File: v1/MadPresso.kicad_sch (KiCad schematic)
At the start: 38 parts, among them J1 Conn_01x07, J2 Conn_01x03, Q1 2N7002, Q2 2N7002, Q3 BC847, U1 LTV-356T, U2 WeMos_mini

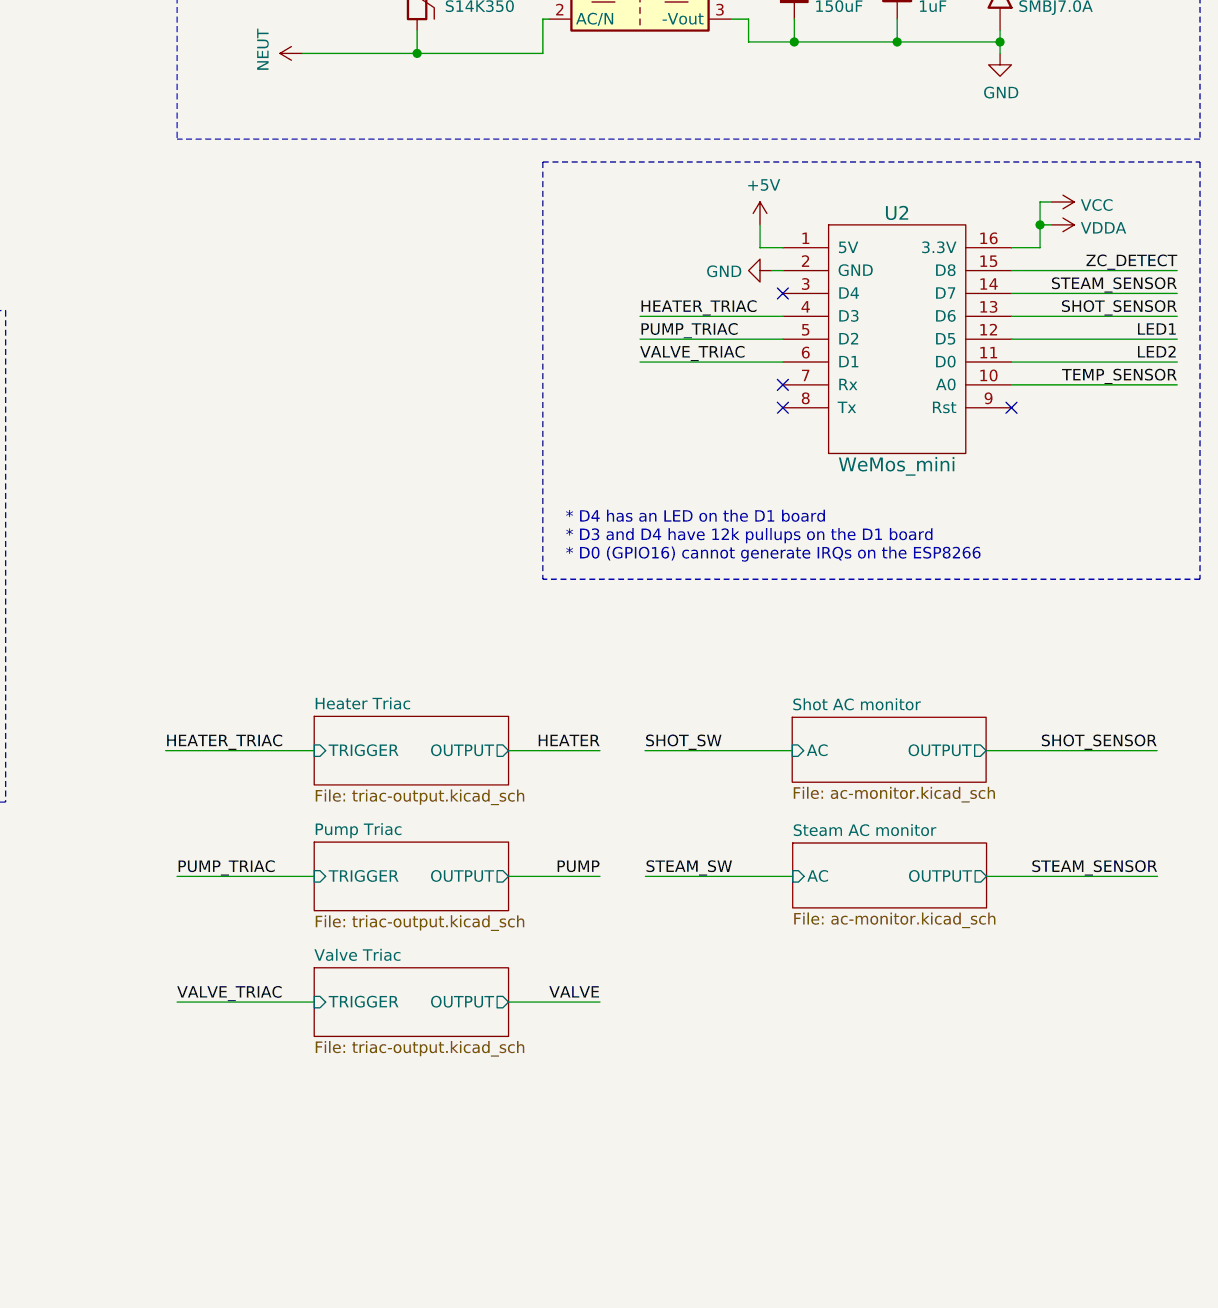
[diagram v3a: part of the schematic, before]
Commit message: Update to new KiCad symbols, replace and turn D1 module
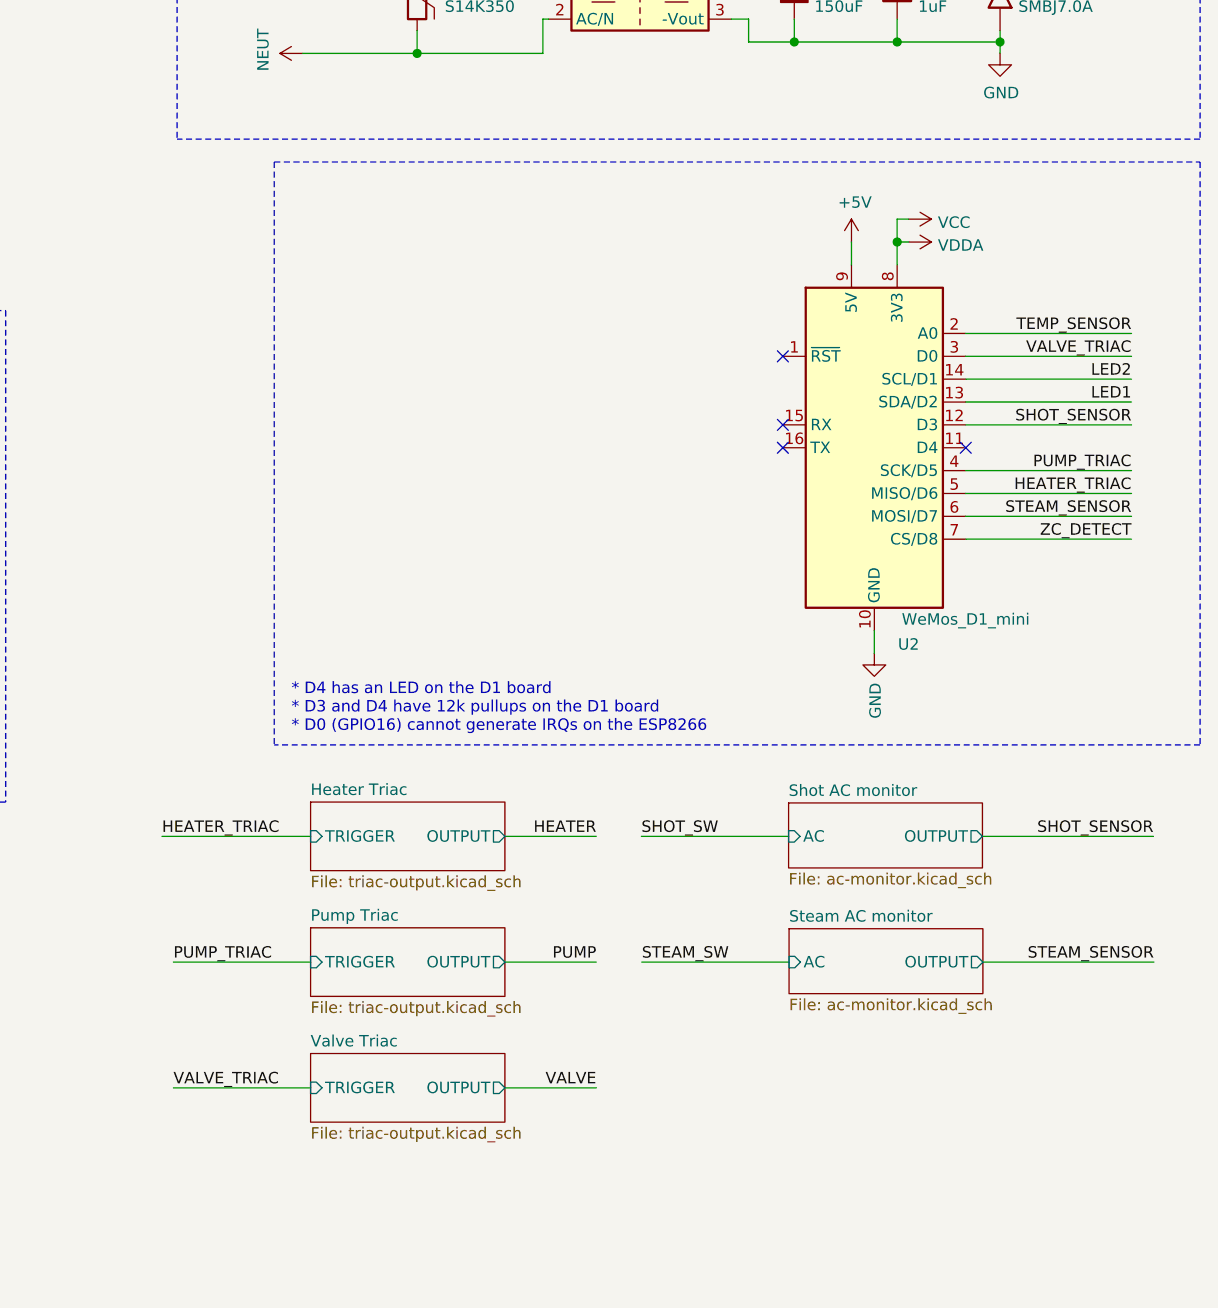
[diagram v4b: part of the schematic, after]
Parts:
- removed U2: WeMos_mini, wemos_d1_mini:D1_mini_board, symbol CofeePID-rescue:WeMos_mini-wemos_mini
- added U2: WeMos_D1_mini, Module:WEMOS_D1_mini_light, symbol MCU_Module:WeMos_D1_mini
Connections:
- net +5V: now also U2.9 (5V)
- net GND: now also U2.10 (GND)
- net HEATER_TRIAC: now also U2.5 (MISO/D6)
- net LED1: now also U2.13 (SDA/D2)
- net LED2: now also U2.14 (SCL/D1)
- net PUMP_TRIAC: now also U2.4 (SCK/D5)
- net SHOT_SENSOR: now also U2.12 (D3)
- net STEAM_SENSOR: now also U2.6 (MOSI/D7)
- net TEMP_SENSOR: now also U2.2 (A0)
- net VALVE_TRIAC: now also U2.3 (D0)
- net VCC: now also U2.8 (3V3)
- net ZC_DETECT: now also U2.7 (CS/D8)
